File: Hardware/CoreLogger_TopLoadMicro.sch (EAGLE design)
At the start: 75 parts, among them J1 CONN_32.54_SCREW, J10 CONN_42.54_SCREW, J11 CONN_32.54_SCREW, J12 CONN_32.54_SCREW, J13 CONN_62.54, J2 CONN_32.54_SCREW, J4 CONN_5, J6 CONN_42.54_SCREW, J7 CONN_42.54_SCREW, J8 CONN_42.54_SCREW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

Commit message: Generated optional board designs, generated gerbers
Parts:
- removed R41: 10k, bschulz_passives:R-EU_10KR0402
- SD1: value MICROSDCD -> MICROSD_NOCDHINDGED; device bschulz:MICROSDCD -> bschulz:MICROSD_NOCDHINDGED
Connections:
- net 3V3: no longer R41.2
- net GND: no longer SD1.CARD_DETECT1
- net SD_CD: no longer R41.1, SD1.CARD_DETECT
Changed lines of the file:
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@@
 <part name="GND28" library="supply1" library_urn="urn:adsk.eagle:library:371" deviceset="GND" device=""/>
 <part name="C10" library="bschulz_passives" deviceset="C-EU" device="C0603" technology="0.1UF" value="0.1uF"/>
-<part name="SD1" library="bschulz" deviceset="MICROSD" device="CD" value="MICROSDCD"/>
+<part name="SD1" library="bschulz" deviceset="MICROSD_NOCD" device="HINDGED" value="MICROSD_NOCDHINDGED"/>
 <part name="GND44" library="supply1" library_urn="urn:adsk.eagle:library:371" deviceset="GND" device=""/>
-<part name="R41" library="bschulz_passives" deviceset="R-EU_" device="R0402" technology="10K" value="10k"/>
-<part name="GND43" library="supply1" library_urn="urn:adsk.eagle:library:371" deviceset="GND" device=""/>
 <part name="J11" library="bschulz" deviceset="CONN_3" device="2.54_SCREW"/>
 <part name="J12" library="bschulz" deviceset="CONN_3" device="2.54_SCREW"/>
@@
 <attribute name="VALUE" x="60.96" y="327.66" size="1.778" layer="96"/>
 </instance>
-<instance part="R41" gate="G$1" x="17.78" y="345.44" smashed="yes" rot="R90">
-<attribute name="NAME" x="16.2814" y="341.63" size="1.778" layer="95" rot="R90"/>
-<attribute name="VALUE" x="21.082" y="341.63" size="1.778" layer="96" rot="R90"/>
-</instance>
-<instance part="GND43" gate="1" x="30.48" y="322.58" smashed="yes">
-<attribute name="VALUE" x="27.94" y="320.04" size="1.778" layer="96"/>
-</instance>
 <instance part="R13" gate="G$1" x="-15.24" y="50.8" smashed="yes" rot="R90">
 <attribute name="NAME" x="-16.7386" y="46.99" size="1.778" layer="95" rot="R90"/>
@@
 </segment>
 <segment>
-<pinref part="SD1" gate="G$1" pin="CARD_DETECT1"/>
-<pinref part="GND43" gate="1" pin="GND"/>
-<wire x1="30.48" y1="340.36" x2="30.48" y2="325.12" width="0.1524" layer="91"/>
-</segment>
-<segment>
 <pinref part="C11" gate="G$1" pin="2"/>
 <wire x1="175.26" y1="248.92" x2="175.26" y2="246.38" width="0.1524" layer="91"/>
@@
 <wire x1="55.88" y1="340.36" x2="55.88" y2="335.28" width="0.1524" layer="91"/>
 <label x="55.88" y="335.28" size="0.8128" layer="95" rot="R270" xref="yes"/>
-</segment>
-<segment>
-<pinref part="R41" gate="G$1" pin="2"/>
-<wire x1="17.78" y1="350.52" x2="17.78" y2="353.06" width="0.1524" layer="91"/>
-<wire x1="17.78" y1="353.06" x2="15.24" y2="353.06" width="0.1524" layer="91"/>
-<label x="15.24" y="353.06" size="0.8128" layer="95" rot="R180" xref="yes"/>
 </segment>
 <segment>
@@
 <net name="SD_CD" class="0">
 <segment>
-<pinref part="SD1" gate="G$1" pin="CARD_DETECT"/>
-<pinref part="R41" gate="G$1" pin="1"/>
-<wire x1="27.94" y1="340.36" x2="17.78" y2="340.36" width="0.1524" layer="91"/>
-<wire x1="27.94" y1="340.36" x2="27.94" y2="335.28" width="0.1524" layer="91"/>
-<junction x="27.94" y="340.36"/>
-<label x="27.94" y="335.28" size="0.8128" layer="95" rot="R270" xref="yes"/>
-</segment>
-<segment>
 <pinref part="U11" gate="G$1" pin="GPB5"/>

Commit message: Added BoM info and software for Lidar Lite interface
Updated the BoM information in Eagle and generated csv, also added software for LidarLite interface system
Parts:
- C9: device bschulz_passives:C-EUC0603 -> bschulz_passives:C-EU1NFC0603
- D1: DIGIKEY (none) -> 1N4448WTPMSCT-ND; MF (none) -> Micro Commercial; MPN (none) -> 1N4448W-TP
- L1: DIGIKEY (none) -> 732-10757-1-ND; MF (none) -> Wurth; MPN (none) -> 74404043100A
- R10, R11: value 10M -> 180k; device bschulz_passives:R-EU_10MR0603 -> bschulz_passives:R-EU_180KR0603
- R12: device bschulz_passives:R-EU_R0805 -> bschulz_passives:R-EU_0.1R0805
- R3: device bschulz_passives:R-EU_R0603 -> bschulz_passives:R-EU_422KR0603
- R5, R8: device bschulz_passives:R-EU_R0603 -> bschulz_passives:R-EU_1KR0603
- R6: device bschulz_passives:R-EU_R0603 -> bschulz_passives:R-EU_470R0603
- R7: device bschulz_passives:R-EU_R0603 -> bschulz_passives:R-EU_P27KR0603
- R9: device bschulz_passives:R-EU_R0805 -> bschulz_passives:R-EU_0.01R0805
- VR1: DIGIKEY (none) -> 3214W-1-204ECT-ND; MF (none) -> Bourns; MPN (none) -> 3214W-1-204E
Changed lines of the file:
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@@
 <?xml version="1.0" encoding="utf-8"?>
 <!DOCTYPE eagle SYSTEM "eagle.dtd">
-<eagle version="9.3.0">
+<eagle version="9.2.1">
 <drawing>
 <settings>
@@
 <layer number="18" name="Vias" color="2" fill="1" visible="yes" active="no"/>
 <layer number="19" name="Unrouted" color="6" fill="1" visible="yes" active="no"/>
-<layer number="20" name="Dimension" color="15" fill="1" visible="yes" active="no"/>
+<layer number="20" name="Dimension" color="24" fill="1" visible="yes" active="no"/>
 <layer number="21" name="tPlace" color="7" fill="1" visible="yes" active="no"/>
 <layer number="22" name="bPlace" color="7" fill="1" visible="yes" active="no"/>
@@
 <part name="MS1" library="adafruit" library_urn="urn:adsk.eagle:library:420" deviceset="FEATHERWING" device="_NODIM" value="FEATHERWING_NODIM"/>
 <part name="U1" library="bschulz" deviceset="TPS6220*" device="SOT23" technology="0"/>
-<part name="VR1" library="bschulz" deviceset="POTENTIOMETER" device="3214W"/>
-<part name="L1" library="bschulz" deviceset="INDUCTOR" device="LQS_4X4" value="10uH"/>
+<part name="VR1" library="bschulz" deviceset="POTENTIOMETER" device="3214W">
+<attribute name="DIGIKEY" value="3214W-1-204ECT-ND"/>
+<attribute name="MF" value="Bourns"/>
+<attribute name="MPN" value="3214W-1-204E"/>
+</part>
+<part name="L1" library="bschulz" deviceset="INDUCTOR" device="LQS_4X4" value="10uH">
+<attribute name="DIGIKEY" value="732-10757-1-ND"/>
+<attribute name="MF" value="Wurth"/>
+<attribute name="MPN" value="74404043100A"/>
+</part>
 <part name="C1" library="bschulz_passives" deviceset="C-EU" device="C0402" technology="56PF" value="56pF"/>
 <part name="C2" library="bschulz_passives" deviceset="C-EU" device="C0402" technology="220PF" value="220pF"/>
-<part name="R3" library="bschulz_passives" deviceset="R-EU_" device="R0603" value="442k"/>
+<part name="R3" library="bschulz_passives" deviceset="R-EU_" device="R0603" technology="422K" value="442k"/>
 <part name="R4" library="bschulz_passives" deviceset="R-EU_" device="R0603" technology="180K" value="180k"/>
 <part name="GND1" library="supply1" library_urn="urn:adsk.eagle:library:371" deviceset="GND" device=""/>
@@
 <part name="GND4" library="supply1" library_urn="urn:adsk.eagle:library:371" deviceset="GND" device=""/>
 <part name="Q1" library="bschulz" deviceset="MOSFET-NCH" device="-DMG3404L" value="DMG3404"/>
-<part name="D1" library="bschulz" deviceset="DIODE" device="SOD-123"/>
+<part name="D1" library="bschulz" deviceset="DIODE" device="SOD-123">
+<attribute name="DIGIKEY" value="1N4448WTPMSCT-ND"/>
+<attribute name="MF" value="Micro Commercial"/>
+<attribute name="MPN" value="1N4448W-TP"/>
+</part>
 <part name="GND5" library="supply1" library_urn="urn:adsk.eagle:library:371" deviceset="GND" device=""/>
 <part name="U3" library="bschulz" deviceset="MIC2544" device="MSOP"/>
@@
 <part name="C6" library="bschulz_passives" deviceset="C-EU" device="C0805" technology="22UF" value="22uF"/>
 <part name="GND8" library="supply1" library_urn="urn:adsk.eagle:library:371" deviceset="GND" device=""/>
-<part name="R5" library="bschulz_passives" deviceset="R-EU_" device="R0603"/>
+<part name="R5" library="bschulz_passives" deviceset="R-EU_" device="R0603" technology="1K"/>
 <part name="U4" library="bschulz" deviceset="MIC2544" device="MSOP"/>
 <part name="C7" library="bschulz_passives" deviceset="C-EU" device="C0402" technology="0.1UF" value="0.1uF"/>
@@
 <part name="C8" library="bschulz_passives" deviceset="C-EU" device="C0805" technology="22UF" value="22uF"/>
 <part name="GND11" library="supply1" library_urn="urn:adsk.eagle:library:371" deviceset="GND" device=""/>
-<part name="R6" library="bschulz_passives" deviceset="R-EU_" device="R0603"/>
+<part name="R6" library="bschulz_passives" deviceset="R-EU_" device="R0603" technology="470"/>
 <part name="U2" library="bschulz" deviceset="SN74AUP1G34" device="SC70"/>
 <part name="GND12" library="supply1" library_urn="urn:adsk.eagle:library:371" deviceset="GND" device=""/>
 <part name="U5" library="bschulz" deviceset="LTC2054" device=""/>
-<part name="R7" library="bschulz_passives" deviceset="R-EU_" device="R0603"/>
-<part name="R8" library="bschulz_passives" deviceset="R-EU_" device="R0603"/>
-<part name="C9" library="bschulz_passives" deviceset="C-EU" device="C0603"/>
+<part name="R7" library="bschulz_passives" deviceset="R-EU_" device="R0603" technology="P27K"/>
+<part name="R8" library="bschulz_passives" deviceset="R-EU_" device="R0603" technology="1K"/>
+<part name="C9" library="bschulz_passives" deviceset="C-EU" device="C0603" technology="1NF"/>
 <part name="GND13" library="supply1" library_urn="urn:adsk.eagle:library:371" deviceset="GND" device=""/>
 <part name="GND14" library="supply1" library_urn="urn:adsk.eagle:library:371" deviceset="GND" device=""/>
@@
 <part name="GND21" library="supply1" library_urn="urn:adsk.eagle:library:371" deviceset="GND" device=""/>
 <part name="U11" library="bschulz" deviceset="MCP23018" device="QFN"/>
-<part name="R10" library="bschulz_passives" deviceset="R-EU_" device="R0603" technology="10M" value="10M"/>
-<part name="R11" library="bschulz_passives" deviceset="R-EU_" device="R0603" technology="10M" value="10M"/>
+<part name="R10" library="bschulz_passives" deviceset="R-EU_" device="R0603" technology="180K" value="180k"/>
+<part name="R11" library="bschulz_passives" deviceset="R-EU_" device="R0603" technology="180K" value="180k"/>
 <part name="P+1" library="supply1" library_urn="urn:adsk.eagle:library:371" deviceset="VCC" device=""/>
 <part name="GND22" library="supply1" library_urn="urn:adsk.eagle:library:371" deviceset="GND" device=""/>
@@
 <part name="U13" library="bschulz" deviceset="INA219" device="DCN"/>
 <part name="GND24" library="supply1" library_urn="urn:adsk.eagle:library:371" deviceset="GND" device=""/>
-<part name="R9" library="bschulz_passives" deviceset="R-EU_" device="R0805" value="10m"/>
+<part name="R9" library="bschulz_passives" deviceset="R-EU_" device="R0805" technology="0.01" value="10m"/>
 <part name="U14" library="bschulz" deviceset="INA219" device="DCN"/>
 <part name="GND25" library="supply1" library_urn="urn:adsk.eagle:library:371" deviceset="GND" device=""/>
-<part name="R12" library="bschulz_passives" deviceset="R-EU_" device="R0805" value="100m"/>
+<part name="R12" library="bschulz_passives" deviceset="R-EU_" device="R0805" technology="0.1" value="100m"/>
 <part name="U$1" library="LEAF_Components" deviceset="POLOLU_REGULATOR" device=""/>
 <part name="GND26" library="supply1" library_urn="urn:adsk.eagle:library:371" deviceset="GND" device=""/>
@@
 <attribute name="NAME" x="177.292" y="84.074" size="1.778" layer="95" font="vector" rot="R90"/>
 <attribute name="VALUE" x="181.61" y="83.82" size="1.778" layer="95" font="vector" rot="R270" align="bottom-center"/>
+<attribute name="MF" x="180.34" y="83.82" size="1.778" layer="96" rot="R180" display="off"/>
+<attribute name="DIGIKEY" x="180.34" y="83.82" size="1.778" layer="96" rot="R180" display="off"/>
+<attribute name="MPN" x="180.34" y="83.82" size="1.778" layer="96" rot="R180" display="off"/>
 </instance>
 <instance part="L1" gate="G$1" x="172.72" y="106.68" smashed="yes" rot="R90">
 <attribute name="NAME" x="177.8" y="105.41" size="1.778" layer="95" rot="R180"/>
 <attribute name="VALUE" x="177.8" y="110.49" size="1.778" layer="96" rot="R180"/>
+<attribute name="MF" x="172.72" y="106.68" size="1.778" layer="96" rot="R90" display="off"/>
+<attribute name="MPN" x="172.72" y="106.68" size="1.778" layer="96" rot="R90" display="off"/>
+<attribute name="DIGIKEY" x="172.72" y="106.68" size="1.778" layer="96" rot="R90" display="off"/>
 </instance>
 <instance part="C1" gate="G$1" x="187.96" y="104.14" smashed="yes">
@@
 <attribute name="NAME" x="225.5774" y="101.6" size="1.778" layer="95" rot="R90"/>
 <attribute name="VALUE" x="228.3714" y="101.6" size="1.778" layer="96" rot="R90"/>
+<attribute name="MF" x="226.06" y="99.06" size="1.778" layer="96" rot="R90" display="off"/>
+<attribute name="DIGIKEY" x="226.06" y="99.06" size="1.778" layer="96" rot="R90" display="off"/>
+<attribute name="MPN" x="226.06" y="99.06" size="1.778" layer="96" rot="R90" display="off"/>
 </instance>
 <instance part="GND5" gate="1" x="226.06" y="73.66" smashed="yes">

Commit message: General schematic cleanup on logger board
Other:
- note added: "Connectors and Mechanical"
- note added: "Digital Core"
- note added: "Power"
- note added: "Sensor Interface"
- note removed: "Add 5v converter! Add battery connector! Add current monitor"
- note removed: "Add alternative amp structure?"
- note removed: "Add caps???"
- note removed: "Add counter!"
- note removed: "Add shunt resistor, AMP?????"
- note removed: "Add test points!"
- note removed: "Add test points!!"
- note removed: "Add therm amp!"
- note removed: "Check addresses"
- note removed: "Connect to Paticle!"
- note removed: "Connect to Paticle?"
- note removed: "Pick diode!"
- note removed: "Pullup for input pulse line"
- note removed: "Remove??"
- note removed: "Use alternatite SOIC package?"

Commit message: Minor cleanup
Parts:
- R5: value (none) -> 1k
- R6: value (none) -> 470
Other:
- note added: "I,lim ~= 250mA"
- note added: "I,lim ~= 500mA"
- note added: "OpenLog"
- note added: "Soil Temp 1"
- note added: "Soil Temp 2"
- note removed: "Calc resistors!"
- moved on the sheet: C12, C13, C14, C17, C3, C5, C7, J3, R9, U$1

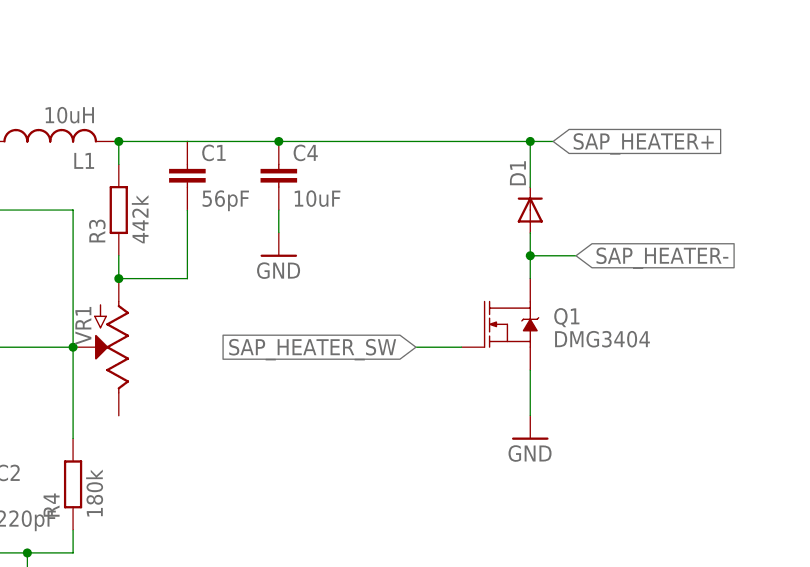
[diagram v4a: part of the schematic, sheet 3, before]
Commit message: Added Sap Heater FET pullup
Added gate pullup to the FET drive on the sap heater power system
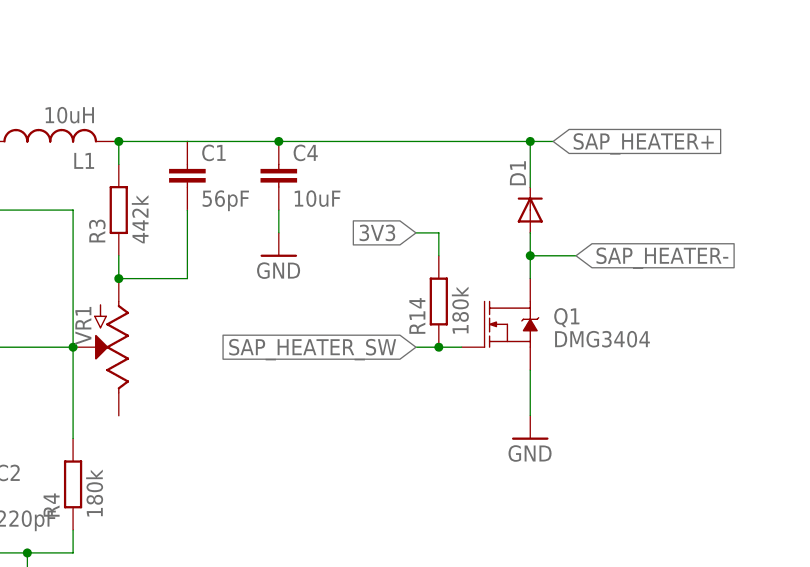
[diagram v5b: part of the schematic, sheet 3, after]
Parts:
- added R14: 180k, bschulz_passives:R-EU_180KR0603
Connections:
- net 3V3: now also R14.2
- net SAP_HEATER_SW: now also R14.1
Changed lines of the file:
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@@
 <setting verticaltext="up"/>
 </settings>
-<grid distance="0.1" unitdist="inch" unit="mm" style="lines" multiple="1" display="no" altdistance="0.01" altunitdist="inch" altunit="mm"/>
+<grid distance="0.1" unitdist="inch" unit="inch" style="lines" multiple="1" display="no" altdistance="0.01" altunitdist="inch" altunit="inch"/>
 <layers>
 <layer number="1" name="Top" color="4" fill="1" visible="no" active="no"/>
@@
 <attribute name="REV" value="0.0"/>
 </part>
+<part name="R14" library="bschulz_passives" deviceset="R-EU_" device="R0603" technology="180K" value="180k"/>
 </parts>
 <sheets>
@@
 <attribute name="REV" x="261.62" y="7.62" size="2.54" layer="94"/>
 </instance>
+<instance part="R14" gate="G$1" x="129.54" y="73.66" smashed="yes" rot="R90">
+<attribute name="NAME" x="128.0414" y="69.85" size="1.778" layer="95" rot="R90"/>
+<attribute name="VALUE" x="132.842" y="69.85" size="1.778" layer="96" rot="R90"/>
+</instance>
 </instances>
 <busses>
@@
 <segment>
 <pinref part="Q1" gate="NMOS" pin="G"/>
-<wire x1="132.08" y1="68.58" x2="127" y2="68.58" width="0.1524" layer="91"/>
+<wire x1="132.08" y1="68.58" x2="129.54" y2="68.58" width="0.1524" layer="91"/>
 <label x="127" y="68.58" size="1.778" layer="95" rot="R180" xref="yes"/>
+<pinref part="R14" gate="G$1" pin="1"/>
+<wire x1="129.54" y1="68.58" x2="127" y2="68.58" width="0.1524" layer="91"/>
+<junction x="129.54" y="68.58"/>
 </segment>
 </net>
@@
 <label x="243.84" y="170.18" size="1.778" layer="95" xref="yes"/>
 </segment>
-</net>
+<segment>
+<pinref part="R14" gate="G$1" pin="2"/>
+<wire x1="129.54" y1="78.74" x2="129.54" y2="81.28" width="0.1524" layer="91"/>
+<label x="127" y="81.28" size="1.778" layer="95" rot="R180" xref="yes"/>
+<wire x1="129.54" y1="81.28" x2="127" y2="81.28" width="0.1524" layer="91"/>
+</segment>
+</net>
